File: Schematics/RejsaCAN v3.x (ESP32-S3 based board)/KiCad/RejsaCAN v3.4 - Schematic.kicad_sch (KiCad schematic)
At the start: 65 parts, among them Q1 SS8050, U1 ESP32-S3-WROOM-1(N16R8), U2 SN65HVD230DR, U3 ME2807A33M3G, U4 LMR14006XDDCR, U5 MT9700

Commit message: Correct three footprints to the land patterns actually fabricated
Measured from the v3.4 manufacturing data -- top-copper flashes for the pads,
the NPTH drill file for the board locks -- rather than trusted from the stock
libraries:

  F1     pad pitch 3.706mm and 1.407 x 3.500 pads; KiCad's 1812 land is 4.276mm
  U2     SOIC-8 rows 5.544mm apart with 2.045 x 0.588 pads, not 4.95 / 1.95x0.60
  USBC1  shell legs 1.067 and 5.267mm below the contact row (library said 0.600
         and 4.800); NPTH board locks 1.676mm below it (library said 1.120)

All three now sit on their original pads to 0-1 um, and board pad coverage rises
from 216 to 225 of 232. F1 and U2 move to project-local footprints so the fix
cannot be silently undone by a library update; the schematic's footprint fields
move with them, verified by re-exporting the BOM.

This clears every electrical DRC violation. The two that remained were caused by
the wrong geometry: with U2's real 2.045mm pads it comes within 0.189mm of C11,
which is the board that was actually built and is inside JLCPCB's 0.15mm SMD
pad-to-pad floor. A third custom rule allows that spacing between pads while
keeping the full net-class clearance for tracks and vias -- component choice
sets pad spacing, the router should not be let off the same hook.

Remaining DRC is non-electrical: silkscreen text overlaps, courtyard overlaps
(KiCad's courtyards are more generous than EasyEDA's), and the top two mounting
holes falling in the stock module footprint's antenna keepout.

Co-Authored-By: Claude Opus 5 (1M context) <noreply@anthropic.com>
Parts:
- F1: footprint Fuse:Fuse_1812_4532Metric -> RejsaCAN:Fuse_1812_RejsaCAN_3.706mm
- U2: footprint Package_SO:SOIC-8_3.9x4.9mm_P1.27mm -> RejsaCAN:SOIC-8_RejsaCAN_5.544mm
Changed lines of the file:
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@@
 			)
 		)
-		(property "Footprint" "Fuse:Fuse_1812_4532Metric"
+		(property "Footprint" "RejsaCAN:Fuse_1812_RejsaCAN_3.706mm"
 			(at 218.44 109.22 0)
 			(hide yes)
@@
 			)
 		)
-		(property "Footprint" "Package_SO:SOIC-8_3.9x4.9mm_P1.27mm"
+		(property "Footprint" "RejsaCAN:SOIC-8_RejsaCAN_5.544mm"
 			(at 180.34 22.86 0)
 			(hide yes)

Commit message: Enlarge U1's thermal vias to 0.3mm, clearing the last sub-tier feature
The stock ESP32-S3-WROOM-1 footprint drills its 12 thermal vias at 0.2mm, the
only feature left under JLCPCB's economical thresholds. Smallest drill on the
board is now 0.300mm, so both limits are satisfied: 5.9 mil minimum trace and
0.3mm minimum hole.

My earlier worry that this would trade one problem for another was based on a
mis-estimated pitch, read off rounded DRC coordinates. Measured properly the
vias sit on a 0.99mm pitch, so a 0.3mm drill still leaves a 0.69mm hole-to-hole
gap against JLCPCB's 0.45mm guidance -- no trade-off at all.

Only the drill changed. Growing the pad to 0.7mm as well (for a wider annular
ring) pushed a B.Cu MTDI track inside the GND clearance, so the pad stays at
0.6mm, giving a 0.15mm ring -- above this board's 0.13mm rule and far above the
0.05mm implied by JLCPCB's own via spec. One stitching via, placed when the
holes were 0.2mm, ended up 0.222mm from a thermal hole against a 0.25mm
minimum; it was one of 44 and is simply removed.

U1 moves to a project-local footprint so a library update cannot silently put
the 0.2mm drills back, matching the treatment F1 and U2 already had, and the
schematic's footprint field moves with it.

DRC: no electrical or fabrication violations. One cosmetic
lib_footprint_mismatch on U1 remains unresolved -- pad count, drills, pad sizes,
attributes, properties and 3D model all verify identical between board and
library, and fabrication output derives from the board, so it affects nothing
that gets manufactured.

Co-Authored-By: Claude Opus 5 (1M context) <noreply@anthropic.com>
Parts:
- U1: footprint RF_Module:ESP32-S3-WROOM-1 -> RejsaCAN:ESP32-S3-WROOM-1_RejsaCAN
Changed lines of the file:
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@@
 			)
 		)
-		(property "Footprint" "RF_Module:ESP32-S3-WROOM-1"
+		(property "Footprint" "RejsaCAN:ESP32-S3-WROOM-1_RejsaCAN"
 			(at 78.74 41.91 0)
 			(hide yes)

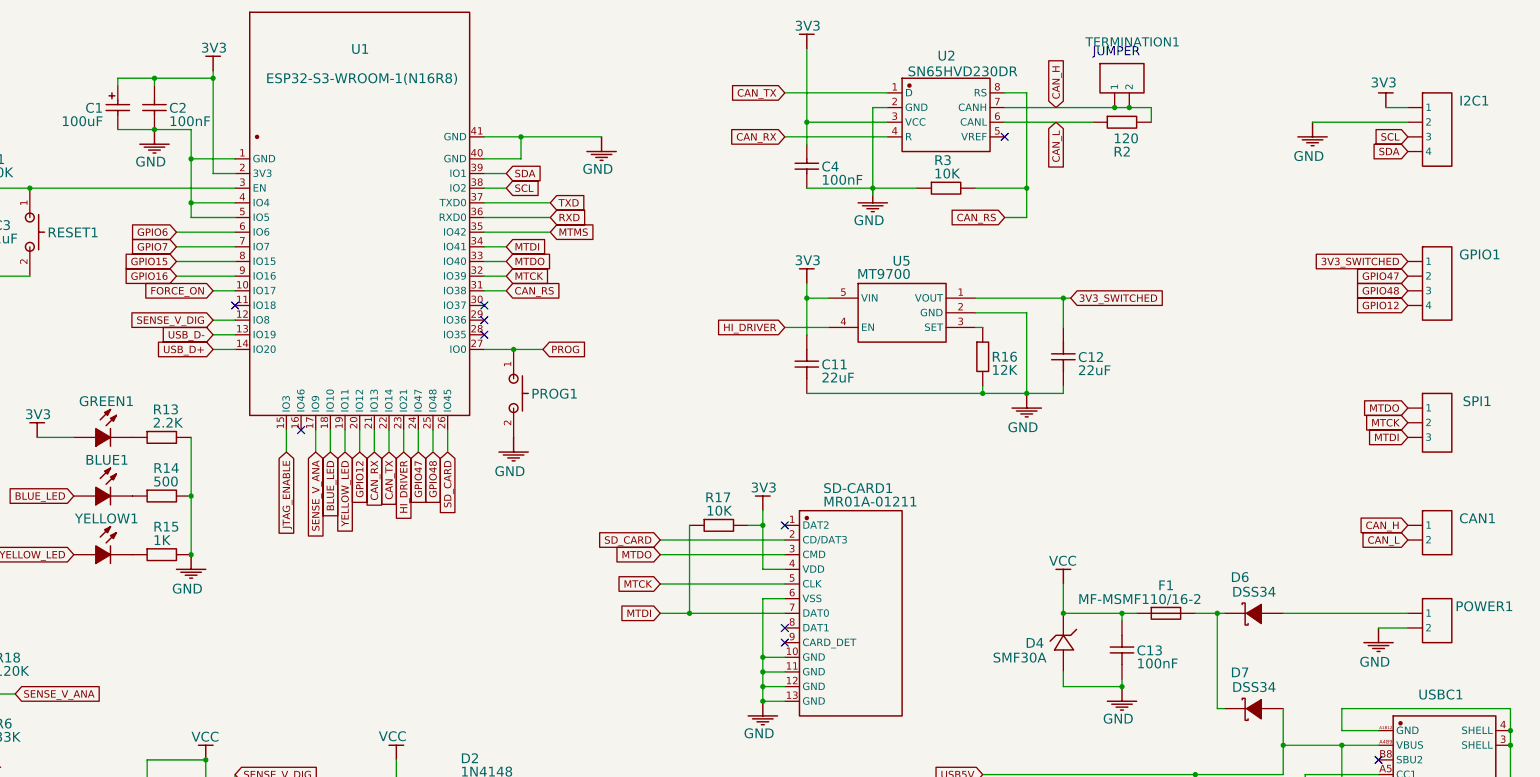
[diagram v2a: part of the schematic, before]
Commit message: Schematic: Micro-Fit input connector and software-switched CAN termination
Replaces the two 2.54mm headers with a single 4-circuit connector, and
turns the cuttable termination link into a GPIO-controlled photorelay.

J1 (Molex Micro-Fit 3.0 43045-0400, 2x02 right-angle) carries 12V, GND,
CAN_H and CAN_L, superseding POWER1 and CAN1. Pins 1 and 2 land on the
existing 12V and GND wires, so the input protection chain is untouched.

Termination was R2 wired permanently across the bus, opened only by
cutting the copper link between TERMINATION1's two pads. U6 (CPC1018N
photorelay) now sits in that gap: CAN_H -> U6 -> TERM_SW -> R2 -> CAN_L.

The photorelay is bipolar and optically isolated, so the ~2.5V CAN
common mode is a non-issue and a bus fault cannot reach the ESP32 --
the trap that makes a discrete MOSFET switch impractical here, since a
3.3V gate only yields Vgs ~0.8V against a floating 2.5V source.

Control is TERM_EN on GPIO16 (was an unused rear-pad net). R20 500R
gives ~4mA, four times the CPC1018N's 1mA operate current, and reuses
R14's existing part rather than adding a BOM line. R21 10k pulls down
so termination is off at reset, before firmware runs. Holding state
through sleep is gpio_hold_en(); through power-off is NVS re-assert.

ERC 256 -> 251 violations. The one new error, R20 pin 1 "Input pin not
driven", is the EasyEDA symbol pin-type artifact behind all 20 of the
pre-existing ones, not an electrical fault.

PCB layout not yet updated.

Co-Authored-By: Claude Opus 5 <noreply@anthropic.com>
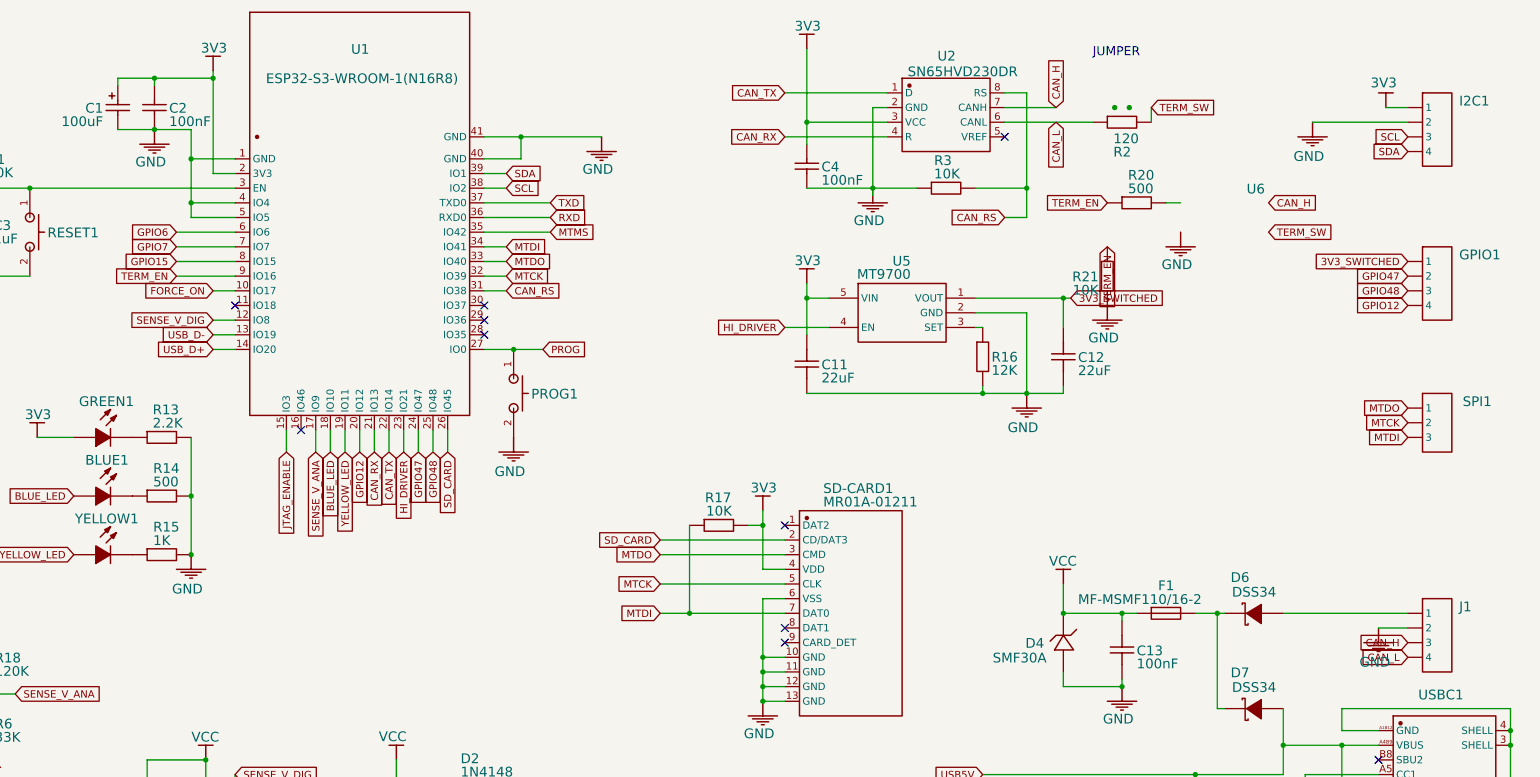
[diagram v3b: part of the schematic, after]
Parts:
- removed CAN1: HDR-M-2.54_1x2, Connector_PinHeader_2.54mm:PinHeader_1x02_P2.54mm_Vertical, symbol HDR-M-2.54_1x2_1
- removed POWER1: HDR-M-2.54_1x2, Connector_PinHeader_2.54mm:PinHeader_1x02_P2.54mm_Vertical, symbol HDR-M-2.54_1x2
- removed TERMINATION1: HDR-M-2.54_1x2, Connector_PinHeader_2.54mm:PinHeader_1x02_P2.54mm_Vertical, symbol HDR-M-2.54_1x2_2
- added J1: Micro-Fit 3.0 4P R/A, Connector_Molex:Molex_Micro-Fit_3.0_43045-0400_2x02_P3.00mm_Horizontal, symbol HDR-M-2.54_1x4_1
- added R20: 500, Resistor_SMD:R_0402_1005Metric, symbol 0402WGF1001TCE_1
- added R21: 10K, Resistor_SMD:R_0402_1005Metric, symbol 0402WGF1002TCE_5
- added U6: CPC1018N, Package_SO:SOP-4_3.8x4.1mm_P2.54mm, symbol CPC1018N
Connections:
- net CAN_H: now also J1.3; no longer R2.2
- net CAN_L: now also J1.4
- net GND: now also J1.2, R21.1
- net at D6.2 (A): now also J1.1
- net GPIO16 renamed TERM_EN
- net TERM_EN: now also R20.1, R21.2
- new net TERM_SW: R2.2

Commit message: Schematic: add LG290P03 GNSS receiver, u.FL antenna and lock LED
U7 is a Quectel LG290P (03) quad-band RTK GNSS module (12.2 x 16.0 x
2.6 mm, 79 pads), talking to the ESP32-S3 over the second UART that
upstream had reserved but never connected.

Connections, all on pins that were previously unused:
  TXD1/RXD1  <-> RXD/TXD  (GPIO44/43) -- module I/O follows VCC, so
                           3.3V logic throughout, no level shifting
  1PPS       ->  GPIO6
  ~RESET     <-  GPIO7
  RTK_STAT   ->  GPS_LOCK: drives GPS1 via R22 1k, and is readable on
                 GPIO15 so firmware can see fix state
  VCC/V_BCKP <-  3V3, decoupled by C27 100nF + C28 22uF

Antenna is an external active type fed from VDD_RF through a bias tee
(L2 into the feed, C30 blocking DC off RF_IN) to J2, a u.FL jack.
C29 bypasses VDD_RF.

Datasheet figures taken from the encrypted Quectel spec supplied by the
user, decrypted locally: VCC 3.0-3.6V typ 3.3V, 99 mA at both
acquisition and tracking, 18 uA backup, UART default 460800 bps.

The vendor KiCad symbol is 2021 format and KiCad 10 rejects its (id N)
and bare hide tokens, so it was converted with kicad-cli sym upgrade
before embedding. Footprint copied into RejsaCAN.pretty per the
project convention for parts with no stock equivalent.

The module's 59 ground pads connect via a vertical rail per side with
an explicit junction at every pin -- a wire passing over a pin does not
connect it in KiCad, which silently cost 59 GND nodes on the first
attempt. GND is now 120 nodes, up from 56.

L2 27nH and C30 100pF are PROVISIONAL: they are standard GNSS bias-tee
values, not yet confirmed against Quectel's hardware design guide.
Do not fabricate before checking them.

ERC 251 -> 291, entirely in the pre-existing benign classes (EasyEDA
pin typing and unregistered-library warnings) plus 13 off-grid
endpoints from vendor symbol pin offsets. Netlist verified per net.

PCB layout still not updated.

Co-Authored-By: Claude Opus 5 <noreply@anthropic.com>
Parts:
- added C27, C29: 100nF, Capacitor_SMD:C_0402_1005Metric, symbol CL05B104KO5NNNC_1
- added C28: 22uF, Capacitor_SMD:C_0603_1608Metric, symbol CL10A226MQ8NRNC_3
- added C30: 100pF, Capacitor_SMD:C_0402_1005Metric, symbol CL05B104KO5NNNC_1
- added GPS1: Blue LED, LED_SMD:LED_0603_1608Metric, symbol 19-217/BHC-ZL1M2RY/3T
- added J2: U.FL, Connector_Coaxial:U.FL_Hirose_U.FL-R-SMT-1_Vertical, symbol HDR-M-2.54_1x2
- added L2: 27nH, Inductor_SMD:L_0402_1005Metric, symbol SLP6028S100MTT
- added R22: 1K, Resistor_SMD:R_0402_1005Metric, symbol 0402WGF1001TCE
- added U7: LG290P03AAMD, RejsaCAN:LG290P03AAMD, symbol LG290P03AAMD
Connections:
- net 3V3: now also C27.2, C28.2
- net GND: now also C27.1, C28.1, C29.1, GPS1.2 (C), J2.2
- net GPIO15 renamed GPS_LOCK
- net GPS_LOCK: now also R22.1
- new net GNSS_ANT: C30.1, J2.1, L2.2
- new net GNSS_LED: GPS1.1 (A), R22.2
- new net GNSS_RF_IN: C30.2
- new net GNSS_VDD_RF: C29.2, L2.1
- no-connect marks 11 -> 18
